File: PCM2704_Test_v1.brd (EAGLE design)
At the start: 44.7 x 30.1 mm, 37 parts, among them X1 USB-MB-S

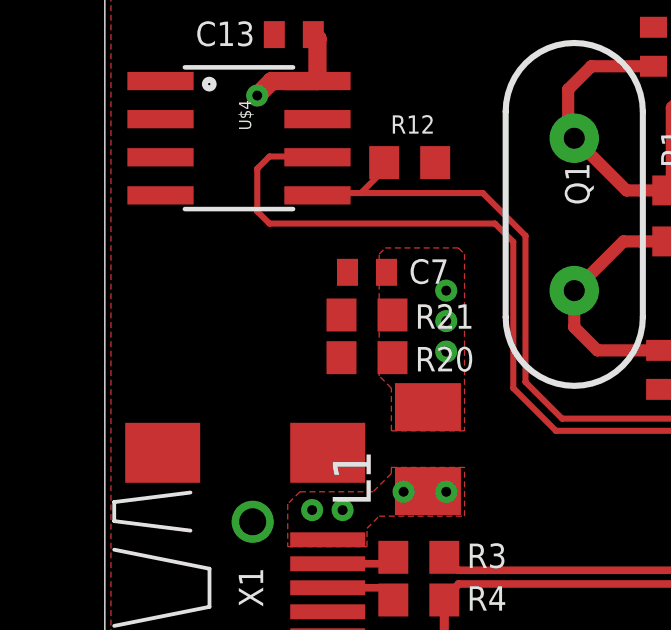
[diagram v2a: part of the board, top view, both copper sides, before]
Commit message: Added LDO for Self-Power
Added an LDO to this design for self-powering the board.
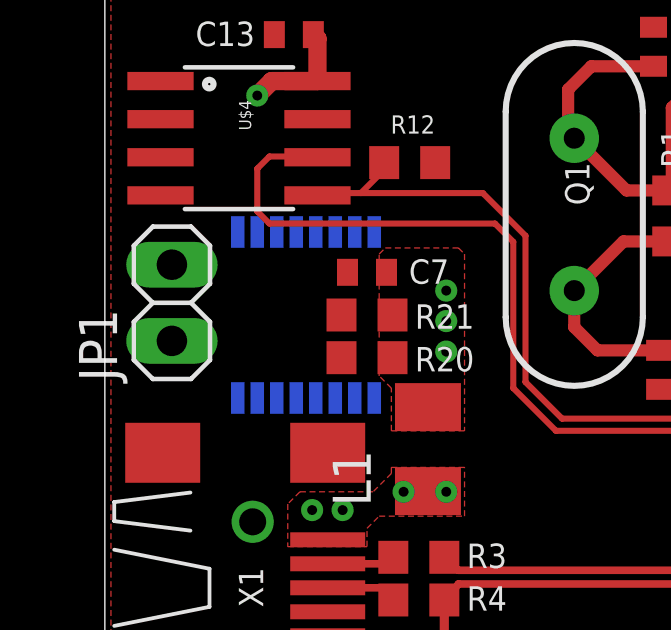
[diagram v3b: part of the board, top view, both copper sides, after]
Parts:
- added IC1: LT1963EFE-3.3, linear-technology:TSSOP16
- added JP1: (no value), pinhead:1X02
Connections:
- new net N$3: IC1.12, IC1.13, IC1.14, JP1.1
- net GND: now also IC1.1, IC1.15, IC1.7, IC1.8, IC1.9, JP1.2
- net VDD: now also IC1.3, IC1.4, IC1.5
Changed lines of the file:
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@@
 <attribute name="VALUE" x="15.4686" y="24.257" size="1.27" layer="27" rot="R180"/>
 </element>
+<element name="IC1" library="linear-technology" package="TSSOP16" value="LT1963EFE-3.3" x="15.24" y="13.0048" rot="MR180">
+<attribute name="OC_NEWARK" value="57M7507" x="15.24" y="13.0048" size="1.778" layer="28" rot="MR180" display="off"/>
+<attribute name="MPN" value="LT1963EFE-3.3" x="15.24" y="13.0048" size="1.778" layer="28" rot="MR180" display="off"/>
+<attribute name="MF" value="" x="15.24" y="13.0048" size="1.778" layer="28" rot="MR180" display="off"/>
+<attribute name="OC_FARNELL" value="unknown" x="15.24" y="13.0048" size="1.778" layer="28" rot="MR180" display="off"/>
+</element>
+<element name="JP1" library="pinhead" package="1X02" value="" x="10.7696" y="13.4112" rot="R90"/>
 </elements>
 <signals>
@@
 <wire x1="35.5998" y1="10.6466" x2="35.3164" y2="10.3632" width="0.3048" layer="1"/>
 <contactref element="C13" pad="2"/>
+<contactref element="IC1" pad="7"/>
+<contactref element="IC1" pad="8"/>
+<contactref element="IC1" pad="9"/>
+<contactref element="IC1" pad="15"/>
+<contactref element="JP1" pad="2"/>
+<contactref element="IC1" pad="1"/>
+<contactref element="IC1" pad="7"/>
+<contactref element="IC1" pad="8"/>
+<contactref element="IC1" pad="9"/>
+<contactref element="IC1" pad="15"/>
 <wire x1="42.3672" y1="21.4732" x2="47.8892" y2="21.5392" width="0" layer="19" extent="1-1"/>
 <wire x1="36.7792" y1="22.7584" x2="42.3672" y2="21.4732" width="0" layer="19" extent="1-1"/>
@@
 <wire x1="47.0408" y1="3.7744" x2="43.2816" y2="3.9776" width="0" layer="19" extent="1-1"/>
 <wire x1="50.2416" y1="8.1292" x2="47.0408" y2="3.7744" width="0" layer="19" extent="1-1"/>
-<wire x1="16.422" y1="11.5824" x2="27.0256" y2="10.526" width="0" layer="19" extent="1-1"/>
+<wire x1="17.515" y1="10.237" x2="27.0256" y2="10.526" width="0" layer="19" extent="1-16"/>
+<wire x1="16.422" y1="11.5824" x2="17.515" y2="10.237" width="0" layer="19" extent="1-16"/>
 <wire x1="16.422" y1="13.0048" x2="16.422" y2="11.5824" width="0" layer="19" extent="1-1"/>
 <wire x1="16.622" y1="14.4272" x2="16.422" y2="13.0048" width="0" layer="19" extent="1-1"/>
-<wire x1="15.621" y1="19.5326" x2="16.622" y2="14.4272" width="0" layer="19" extent="1-1"/>
+<wire x1="16.865" y1="15.7726" x2="16.622" y2="14.4272" width="0" layer="19" extent="1-16"/>
+<wire x1="17.515" y1="15.7726" x2="16.865" y2="15.7726" width="0" layer="19" extent="16-16"/>
+<wire x1="13.615" y1="10.237" x2="16.422" y2="11.5824" width="0" layer="19" extent="1-16"/>
+<wire x1="12.965" y1="15.7726" x2="16.622" y2="14.4272" width="0" layer="19" extent="1-16"/>
+<wire x1="10.7696" y1="14.6812" x2="12.965" y2="15.7726" width="0" layer="19" extent="16-16"/>
+<wire x1="10.3886" y1="16.9926" x2="10.7696" y2="14.6812" width="0" layer="19" extent="1-1"/>
+<wire x1="10.3886" y1="18.2626" x2="10.3886" y2="16.9926" width="0" layer="19" extent="1-1"/>
+<wire x1="10.3886" y1="19.5326" x2="10.3886" y2="18.2626" width="0" layer="19" extent="1-1"/>
+<wire x1="10.3886" y1="20.8026" x2="10.3886" y2="19.5326" width="0" layer="19" extent="1-1"/>
+<wire x1="15.621" y1="19.5326" x2="16.865" y2="15.7726" width="0" layer="19" extent="1-16"/>
 <wire x1="14.1836" y1="22.352" x2="15.621" y2="19.5326" width="0" layer="19" extent="1-1"/>
-<wire x1="10.3886" y1="20.8026" x2="14.1836" y2="22.352" width="0" layer="19" extent="1-1"/>
-<wire x1="10.3886" y1="19.5326" x2="10.3886" y2="20.8026" width="0" layer="19" extent="1-1"/>
-<wire x1="10.3886" y1="18.2626" x2="10.3886" y2="19.5326" width="0" layer="19" extent="1-1"/>
-<wire x1="10.3886" y1="16.9926" x2="10.3886" y2="18.2626" width="0" layer="19" extent="1-1"/>
-<wire x1="15.962" y1="2.3116" x2="16.422" y2="11.5824" width="0" layer="19" extent="1-1"/>
+<wire x1="15.962" y1="2.3116" x2="17.515" y2="10.237" width="0" layer="19" extent="1-16"/>
 </signal>
 <signal name="VDD">
@@
 <wire x1="32.9998" y1="12.46" x2="32.9998" y2="9.1342" width="0.4064" layer="1"/>
 <wire x1="32.9998" y1="9.1342" x2="32.5524" y2="8.6868" width="0.4064" layer="1"/>
+<contactref element="IC1" pad="3"/>
+<contactref element="IC1" pad="5"/>
+<contactref element="IC1" pad="4"/>
 <wire x1="34.2998" y1="20.56" x2="36.8998" y2="20.56" width="0" layer="19" extent="1-1"/>
 <wire x1="32.9184" y1="24.4212" x2="34.3408" y2="23.3276" width="0" layer="19" extent="1-1"/>
@@
 <wire x1="19.5444" y1="18.0848" x2="30.0736" y2="24.4212" width="0" layer="19" extent="1-1"/>
 <wire x1="15.621" y1="20.8026" x2="19.5444" y2="18.0848" width="0" layer="19" extent="1-1"/>
-<wire x1="18.1492" y1="1.9304" x2="32.5524" y2="8.6868" width="0" layer="19" extent="1-1"/>
+<wire x1="15.565" y1="15.7726" x2="13.6144" y2="20.32" width="0" layer="19" extent="16-16"/>
+<wire x1="14.915" y1="15.7726" x2="15.565" y2="15.7726" width="0" layer="19" extent="16-16"/>
+<wire x1="14.265" y1="15.7726" x2="14.915" y2="15.7726" width="0" layer="19" extent="16-16"/>
+<wire x1="18.1492" y1="1.9304" x2="15.565" y2="15.7726" width="0" layer="19" extent="1-16"/>
 </signal>
 <signal name="VBUS_RAW">
@@
 <wire x1="15.5956" y1="18.288" x2="15.621" y2="18.2626" width="0.2032" layer="1"/>
 </signal>
+<signal name="N$3">
+<contactref element="JP1" pad="1"/>
+<contactref element="IC1" pad="12"/>
+<contactref element="IC1" pad="13"/>
+<contactref element="IC1" pad="14"/>
+<wire x1="14.915" y1="10.237" x2="15.565" y2="10.237" width="0" layer="19" extent="16-16"/>
+<wire x1="14.265" y1="10.237" x2="14.915" y2="10.237" width="0" layer="19" extent="16-16"/>
+<wire x1="10.7696" y1="12.1412" x2="14.265" y2="10.237" width="0" layer="19" extent="16-16"/>
+</signal>
 </signals>

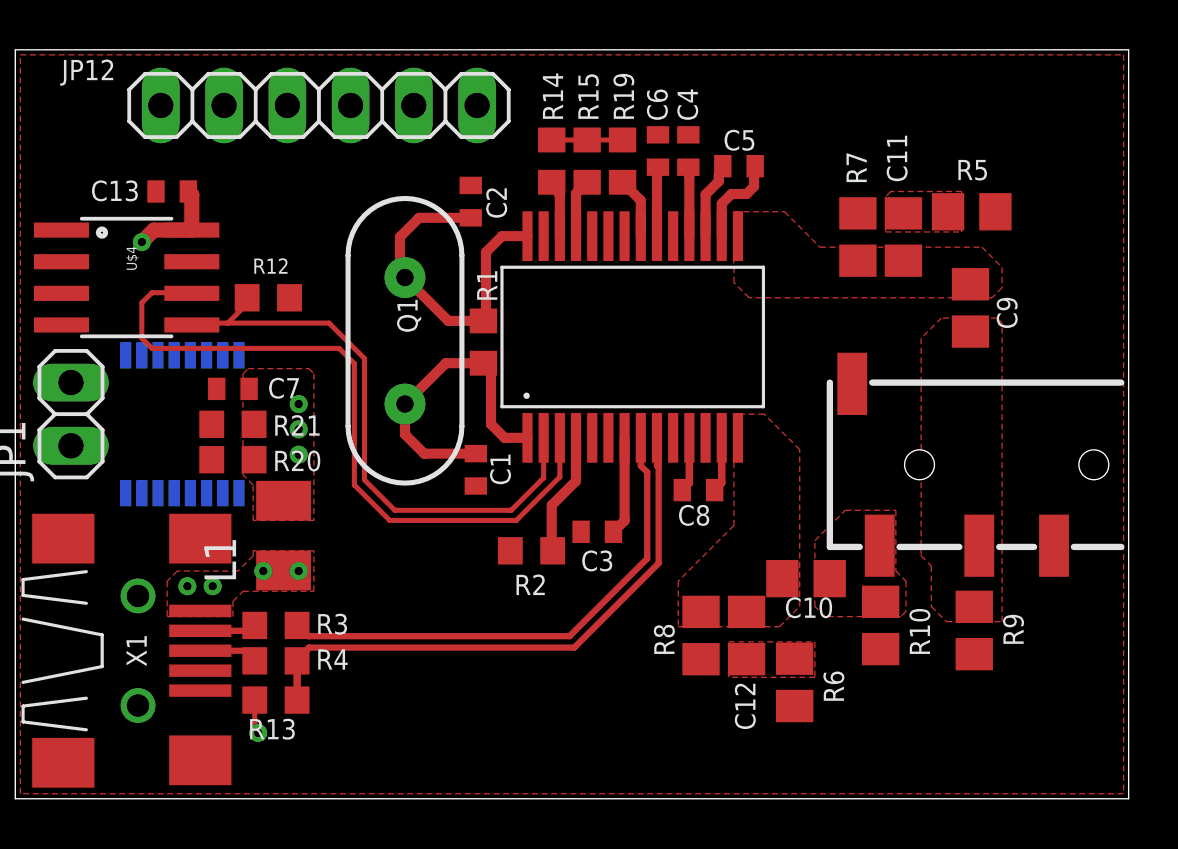
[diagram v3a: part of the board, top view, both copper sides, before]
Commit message: Completed HP Traces
Completed the polygon pour for the headphone jack traces.
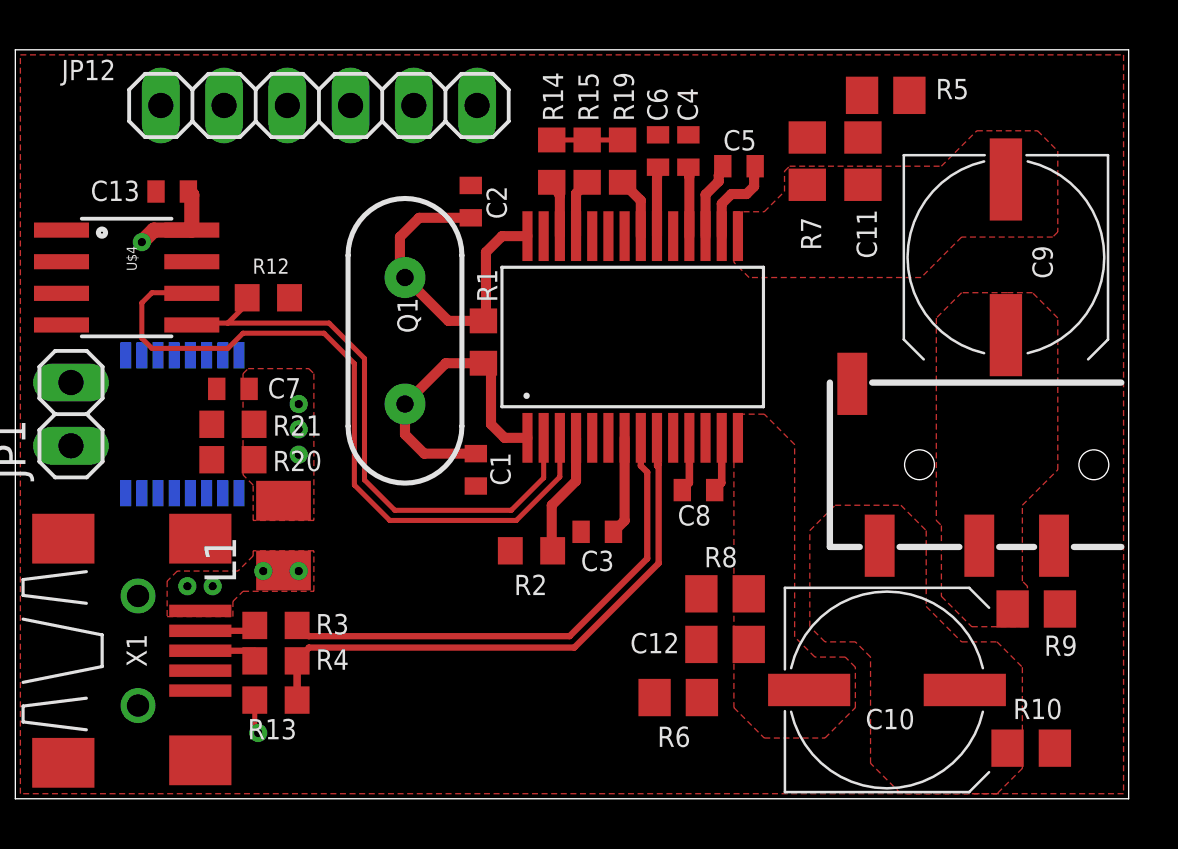
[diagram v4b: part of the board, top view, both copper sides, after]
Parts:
- C10, C9: value 10u -> 100u; device rcl:C0805 -> rcl:UD-8X10_NICHICON
- moved R10 7.80 mm to (49.3, 0.00), turned to 180 degrees
- moved R5 5.81 mm to (43.5, 26.2)
- moved C10 5.53 mm to (43.5, 2.34)
- moved R6 4.71 mm to (35.2, 2.03), turned to 0 degrees
- moved R7 3.66 mm to (40.3, 23.6)
- moved C11 3.45 mm to (42.6, 23.6)
- moved R9 2.63 mm to (49.5, 5.59), turned to 180 degrees
- moved C9 2.48 mm to (48.3, 19.7)
- moved R8 1.93 mm to (37.0, 6.20), turned to 0 degrees
- moved C12 0.93 mm to (37.0, 4.17), turned to 180 degrees
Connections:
- net HP_OUT_L: now also C10.+; no longer C10.2
- net HP_OUT_R: now also C9.+; no longer C9.2
- net VOUTL: now also C10.-; no longer C10.1
- net VOUTR: now also C9.-; no longer C9.1
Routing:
- net N$17: track 28.6 -> 29.1 mm
- removed copper zone on layer 1, net N$19
- removed copper zone on layer 1, net N$20

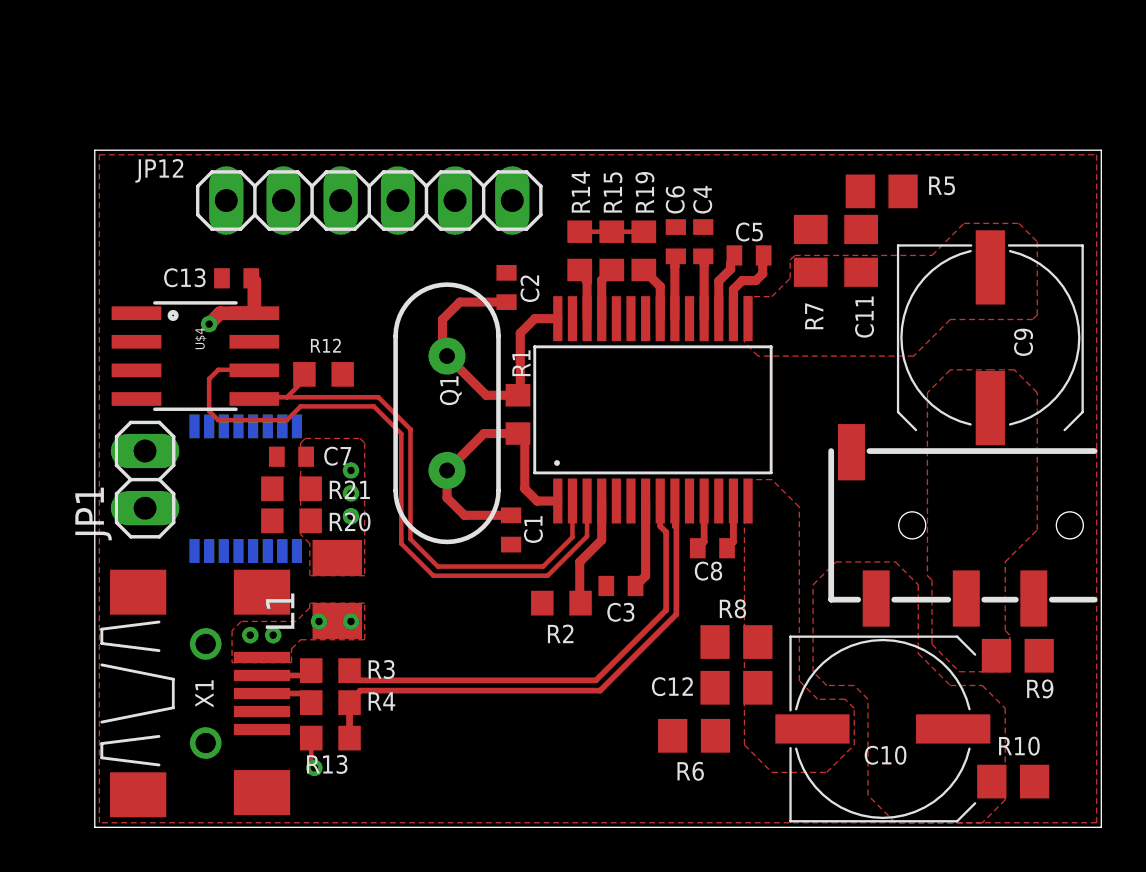
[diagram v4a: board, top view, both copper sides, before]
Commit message: Ran power traces
Ran power traces and moves some components to make room for the power.
Rearranged some resistors to optimize the layout.
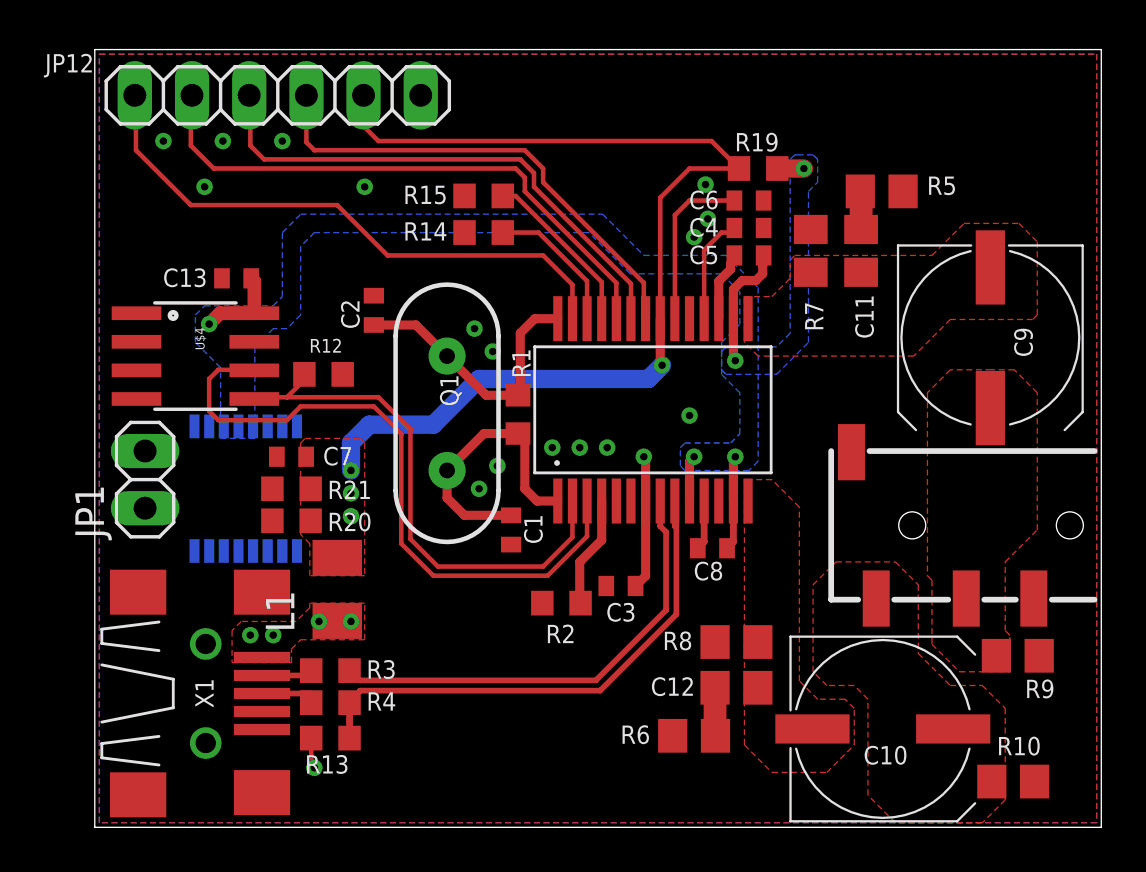
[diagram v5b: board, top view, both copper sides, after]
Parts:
- moved R19 6.26 mm to (38.0, 27.2), turned to 0 degrees
- moved JP12 6.19 mm to (16.7, 30.5)
- moved R15 6.19 mm to (25.8, 26.0), turned to 180 degrees
- moved C2 5.98 mm to (20.9, 20.9)
- moved R14 4.34 mm to (25.8, 24.4), turned to 180 degrees
- moved C6 3.73 mm to (37.6, 25.8), turned to 0 degrees
- moved C4 2.12 mm to (37.6, 24.6), turned to 0 degrees
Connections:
- new net N$4: JP12.2, U$1.24
- new net N$6: JP12.3, U$1.23
- new net N$7: JP12.4, U$1.22
- new net N$9: C6.1, U$1.20
- net GND: now also C6.2; no longer C6.1
- net VDD: no longer C6.2, U$1.20
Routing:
- net VBUS: track 2.46 -> 46.8 mm, vias 3 -> 4
- net SSPND: track 0.00 -> 25.8 mm
- net N$4: track 0.00 -> 25.6 mm
- net N$6: track 0.00 -> 23.6 mm
- net N$7: track 0.00 -> 21.6 mm
- net N$9: track 0.00 -> 7.51 mm
- net N$15: track 2.35 -> 7.60 mm
- net N$14: track 2.25 -> 6.31 mm
- net VDD: track 20.7 -> 24.2 mm, vias 2 -> 7
- net N$20: track 0.00 -> 2.14 mm
- net N$18: track 2.77 -> 4.80 mm
- net N$19: track 0.00 -> 1.71 mm
- net N$2: track 13.7 -> 12.6 mm
- net GND: vias 0 -> 16
- added copper zone on layer 16, net GND
- added copper zone on layer 16, net VDD
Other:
- board size 44.7 x 30.1 mm -> 44.7 x 34.5 mm

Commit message: Completed Board
The board is now complete and ready for printing as soon as it is
reviewed.
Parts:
- added C14: 10u, rc-master-smd:CSV-D
- added C15: 100n, rc-master-smd:C0805
- L1: value (none) -> 10uH
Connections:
- net GND: now also C14.-, C15.1
- net VDD: now also C14.+, C15.2
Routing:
- net VDD: track 24.2 -> 73.7 mm, vias 7 -> 9
- net GND: vias 16 -> 125
- added copper zone on layer 16, net N$3
